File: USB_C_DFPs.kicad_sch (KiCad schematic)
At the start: 34 parts, among them J5 USB_C_Receptacle, J6 USB_C_Receptacle, Q5 IRF7807, U6 LM3478MM_NOPB, U7 SY6280, U8 SY6280

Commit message: Updated schematics
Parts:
- removed C37: 220uF, Capacitor_SMD:CP_Elec_10x10, symbol USB_C_HUB-rescue:CP1-Device
- removed C39: 1nF, Capacitor_SMD:C_0402_1005Metric, symbol Device:C
- removed C40: 22nF, Capacitor_SMD:C_0402_1005Metric, symbol Device:C
- removed C41, C42, C46, C47: 10uF, Capacitor_SMD:C_0603_1608Metric, symbol Device:C_Small
- removed C43: 10pF, Capacitor_SMD:C_0402_1005Metric, symbol Device:C
- removed C44, C45: 100nF, Capacitor_SMD:C_0402_1005Metric, symbol Device:C_Small
- removed C48, C49: 270uF(8mOHM), Capacitor_THT:CP_Radial_D8.0mm_P3.50mm, symbol USB_C_HUB-rescue:CP1-Device
- removed D7: MBRD340, SamacSys_Parts_2:STPS30L30DJFTR, symbol Device:D_Schottky
- removed L2: 1uH_5.6mOHM., Inductor_SMD:L_Sunlord_MWSA1004S, symbol USB_C_HUB-rescue:INDUCTOR_SMALL-OLIMEX_RCL
- removed Q5: IRF7807, symbol Transistor_FET:CSD17579Q5A
- removed R24: 2.55K, Resistor_SMD:R_0603_1608Metric, symbol Device:R_US
- removed R25: 26.7K, Resistor_SMD:R_0603_1608Metric, symbol Device:R_US
- removed R26, R27: 6.8K, Resistor_SMD:R_0603_1608Metric, symbol Device:R_US
- removed R28: 100, Resistor_SMD:R_0603_1608Metric, symbol Device:R_US
- removed R29: 1K, Resistor_SMD:R_0603_1608Metric, symbol Device:R_US
- removed R30: 2.94K, Resistor_SMD:R_0603_1608Metric, symbol Device:R_US
- removed R31: 6m, Resistor_SMD:R_0805_2012Metric, symbol Device:R_US
- removed U6: LM3478MM_NOPB, digikey-footprints:TSSOP-8_W3mm, symbol USB_C_HUB-rescue:LM3478MM_NOPB-dk_PMIC-Voltage-Regulators-DC-DC-Switching-Contr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
- removed U7, U8: SY6280, Package_TO_SOT_SMD:SOT-23-5, symbol USB_C_HUB-rescue:SY6280-usb_hub
- added C37, C41, C42: 0.1μF, Capacitor_SMD:C_0402_1005Metric, symbol Device:C
- added C44, C45: 22μF, Capacitor_SMD:C_0603_1608Metric, symbol Device:C
- added D4: H5VU25U, AZ1045-04F:AZ1045-04F, symbol AZ1045-04F:AZ1045-04F
- added U7: TPS2003CDRCR, DRC10_1P65X2P40_TEX, symbol TPS2003CDRCR:TPS2003CDRCR
- C38: value 100nF -> 0.1μF; LCSC C60474 -> C1525; Part_Number CC0402KRX7R7BB104 -> CL05B104KO5NNNC
- D2, D3: footprint kicad_lceda:DFN2510-10_L2.5-W1.0-P0.50-BL -> AZ1045-04F:AZ1045-04F
- D5: renamed from D4; footprint kicad_lceda:DFN2510-10_L2.5-W1.0-P0.50-BL -> AZ1045-04F:AZ1045-04F
- D6: renamed from D5; footprint kicad_lceda:DFN2510-10_L2.5-W1.0-P0.50-BL -> AZ1045-04F:AZ1045-04F
- D7: renamed from D6; footprint kicad_lceda:DFN2510-10_L2.5-W1.0-P0.50-BL -> AZ1045-04F:AZ1045-04F
- J5, J6: footprint (none) -> USB-C-SMD_TYPE-C-24P-QT:USB-C-SMD_TYPE-C-24P-QT; LCSC (none) -> C2681555; Part_Number (none) -> TYPE-C 24P QT
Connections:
- net +3V3 is gone; now on net USB_DFP1_VBUS: C38.1
- net +5V: now also C42.1, U7.2 (IN)
- net GND: now also C37.2, C41.2, C42.2, C44.2, C45.2, D4.3 (GND), U7.1 (GND), U7.11 (EPAD)
- net USB_DFP0_RX1N: now also D2.5 (I/O_4); no longer D3.4 (I/O_3)
- net USB_DFP0_RX1P: now also D2.4 (I/O_3); no longer D3.5 (I/O_4)
- net USB_DFP0_RX2N: now also D4.1 (I/O_1); no longer D2.4 (I/O_3)
- net USB_DFP0_RX2P: now also D4.2 (I/O_2); no longer D2.5 (I/O_4)
- net USB_DFP0_TX2N: now also D3.4 (I/O_3); no longer D3.2 (I/O_2)
- net USB_DFP0_TX2P: now also D3.5 (I/O_4); no longer D3.1 (I/O_1)
- net USB_DFP0_VBUS: now also C37.1, C45.1, U7.9 (OUT1)
- net USB_DFP1_RX1N: now also D6.2 (I/O_2); no longer D7.4 (I/O_3)
- net USB_DFP1_RX1P: now also D6.1 (I/O_1); no longer D7.5 (I/O_4)
- net USB_DFP1_RX2N: now also D7.1 (I/O_1); no longer D6.4 (I/O_3)
- net USB_DFP1_RX2P: now also D7.2 (I/O_2); no longer D6.5 (I/O_4)
- net USB_DFP1_TX1N: now also D5.5 (I/O_4); no longer D6.2 (I/O_2)
- net USB_DFP1_TX1P: now also D5.4 (I/O_3); no longer D6.1 (I/O_1)
- net USB_DFP1_TX2N: now also D6.4 (I/O_3); no longer D7.2 (I/O_2)
- net USB_DFP1_TX2P: now also D6.5 (I/O_4); no longer D7.1 (I/O_1)
- net USB_DFP1_VBUS: now also C44.1, U7.8 (OUT2)
- removed net USB_DFP0_DM: D5.4 (I/O_3), J5.A7 (D-), J5.B7 (D-)
- removed net USB_DFP0_DP: D5.5 (I/O_4), J5.A6 (D+), J5.B6 (D+)
- removed net USB_DFP1_DM: D5.1 (I/O_1), J6.A7 (D-), J6.B7 (D-)
- removed net USB_DFP1_DP: D5.2 (I/O_2), J6.A6 (D+), J6.B6 (D+)
- new net: C41.1, U7.3 (IN)
- new net USB_DFP0_D1N: D3.2 (I/O_2), J5.A7 (D-)
- new net USB_DFP0_D1P: D3.1 (I/O_1), J5.A6 (D+)
- new net USB_DFP0_D2N: D4.5 (I/O_4), J5.B7 (D-)
- new net USB_DFP0_D2P: D4.4 (I/O_3), J5.B6 (D+)
- new net USB_DFP0_EN: U7.4 (EN1)
- new net USB_DFP0_FLT: U7.10 (*FLT1)
- new net USB_DFP1_D1N: D7.5 (I/O_4), J6.A7 (D-)
- new net USB_DFP1_D1P: D7.4 (I/O_3), J6.A6 (D+)
- new net USB_DFP1_D2N: D5.2 (I/O_2), J6.B7 (D-)
- new net USB_DFP1_D2P: D5.1 (I/O_1), J6.B6 (D+)
- new net USB_DFP1_EN: U7.5 (EN2)
- new net USB_DFP1_FLT: U7.6 (*FLT2)
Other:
- note removed: "Boost Converter 5A 5V"
- note removed: "Iset=6800/rs 1A limit r2=6.8k"
- note removed: "Over-current and short circuit protection"
- note removed: "electrolytic alluminium hv little esr"
- moved on the sheet: J6

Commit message: Continue working on board layout
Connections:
- net GND: now also D2.8 (GND), D3.8 (GND), D4.8 (GND), D5.8 (GND), D6.8 (GND), D7.8 (GND)
- net USB_DFP0_D1N: now also D3.9 (NC)
- net USB_DFP0_D1P: now also D3.10 (NC)
- net USB_DFP0_D2N: now also D4.6 (NC)
- net USB_DFP0_D2P: now also D4.7 (NC)
- net USB_DFP0_RX1N: now also D2.6 (NC)
- net USB_DFP0_RX1P: now also D2.7 (NC)
- net USB_DFP0_RX2N: now also D4.10 (NC)
- net USB_DFP0_RX2P: now also D4.9 (NC)
- net USB_DFP0_TX1N: now also D2.9 (NC)
- net USB_DFP0_TX1P: now also D2.10 (NC)
- net USB_DFP0_TX2N: now also D3.7 (NC)
- net USB_DFP0_TX2P: now also D3.6 (NC)
- net USB_DFP1_D1N: now also D7.6 (NC)
- net USB_DFP1_D1P: now also D7.7 (NC)
- net USB_DFP1_D2N: now also D5.9 (NC)
- net USB_DFP1_D2P: now also D5.10 (NC)
- net USB_DFP1_RX1N: now also D6.9 (NC)
- net USB_DFP1_RX1P: now also D6.10 (NC)
- net USB_DFP1_RX2N: now also D7.10 (NC)
- net USB_DFP1_RX2P: now also D7.9 (NC)
- net USB_DFP1_TX1N: now also D5.6 (NC)
- net USB_DFP1_TX1P: now also D5.7 (NC)
- net USB_DFP1_TX2N: now also D6.7 (NC)
- net USB_DFP1_TX2P: now also D6.6 (NC)

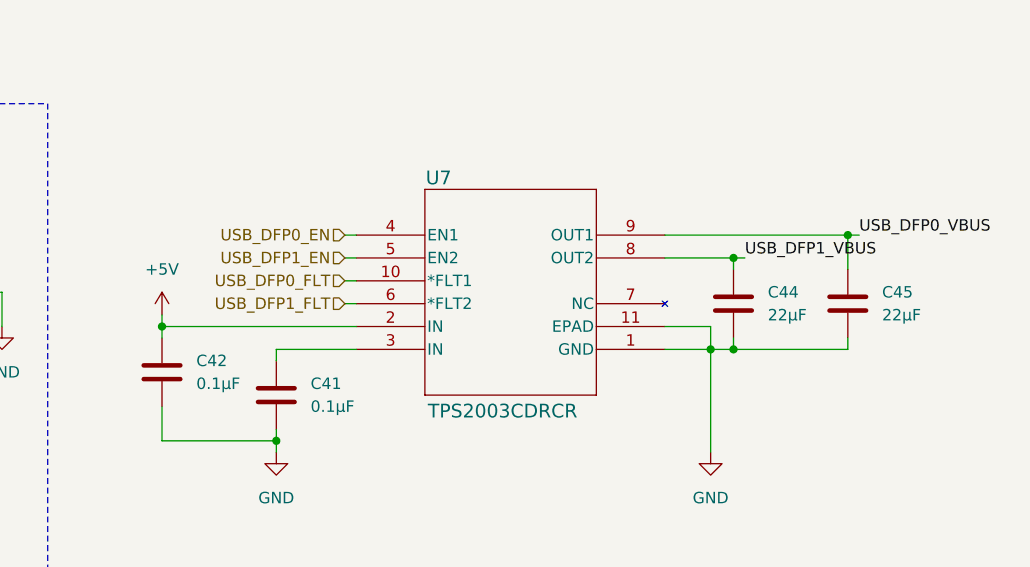
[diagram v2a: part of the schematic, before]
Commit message: Lay out more components
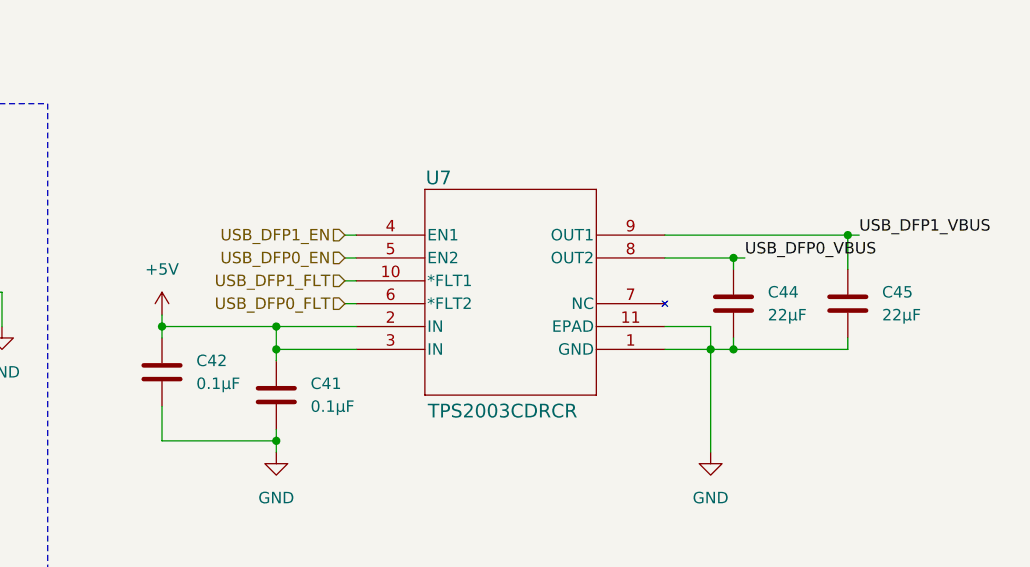
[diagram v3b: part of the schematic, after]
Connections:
- net +5V: now also C41.1, U7.3 (IN)
- net USB_DFP0_EN: now also U7.5 (EN2); no longer U7.4 (EN1)
- net USB_DFP0_FLT: now also U7.6 (*FLT2); no longer U7.10 (*FLT1)
- net USB_DFP0_VBUS: now also C44.1, U7.8 (OUT2); no longer C45.1, U7.9 (OUT1)
- net USB_DFP1_EN: now also U7.4 (EN1); no longer U7.5 (EN2)
- net USB_DFP1_FLT: now also U7.10 (*FLT1); no longer U7.6 (*FLT2)
- net USB_DFP1_VBUS: now also C45.1, U7.9 (OUT1); no longer C44.1, U7.8 (OUT2)
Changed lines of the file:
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@@
+	)
+	(junction
+		(at 200.66 143.51)
+		(diameter 0)
+		(color 0 0 0 0)
 	)
 	(junction
@@
 	)
 	(junction
+		(at 200.66 140.97)
+		(diameter 0)
+		(color 0 0 0 0)
+	)
+	(junction
 		(at 97.79 137.16)
 		(diameter 0)
@@
 	(wire
 		(pts
+			(xy 200.66 140.97) (xy 200.66 143.51)
+		)
+		(stroke
+			(width 0)
+			(type default)
+		)
+	)
+	(wire
+		(pts
 			(xy 86.36 88.9) (xy 90.17 88.9)
 		)
@@
 	(wire
 		(pts
-			(xy 187.96 140.97) (xy 209.55 140.97)
+			(xy 187.96 140.97) (xy 200.66 140.97)
 		)
 		(stroke
@@
 		(pts
 			(xy 45.72 33.02) (xy 49.53 33.02)
+		)
+		(stroke
+			(width 0)
+			(type default)
+		)
+	)
+	(wire
+		(pts
+			(xy 200.66 140.97) (xy 209.55 140.97)
 		)
 		(stroke
@@
 		)
 	)
-	(label "USB_DFP0_VBUS"
+	(label "USB_DFP1_VBUS"
 		(at 265.43 130.81 0)
 		(fields_autoplaced yes)
@@
 		)
 	)
-	(label "USB_DFP1_VBUS"
+	(label "USB_DFP0_VBUS"
 		(at 252.73 133.35 0)
 		(fields_autoplaced yes)
@@
 		)
 	)
-	(hierarchical_label "USB_DFP1_EN"
+	(hierarchical_label "USB_DFP0_EN"
 		(shape input)
 		(at 208.28 133.35 180)
@@
 		)
 	)
-	(hierarchical_label "USB_DFP0_FLT"
+	(hierarchical_label "USB_DFP1_FLT"
 		(shape input)
 		(at 208.28 135.89 180)
@@
 		)
 	)
-	(hierarchical_label "USB_DFP1_FLT"
+	(hierarchical_label "USB_DFP0_FLT"
 		(shape input)
 		(at 208.28 138.43 180)
@@
 		)
 	)
-	(hierarchical_label "USB_DFP0_EN"
+	(hierarchical_label "USB_DFP1_EN"
 		(shape input)
 		(at 208.28 130.81 180)

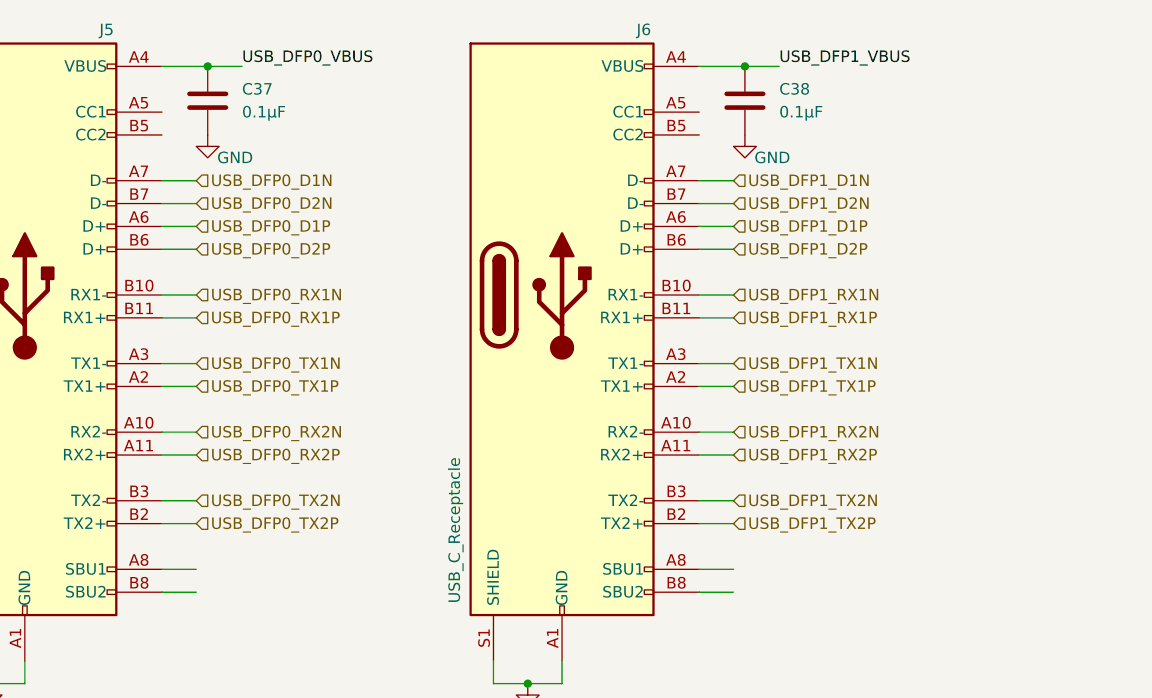
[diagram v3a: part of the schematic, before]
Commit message: Add CC values to DFP ports
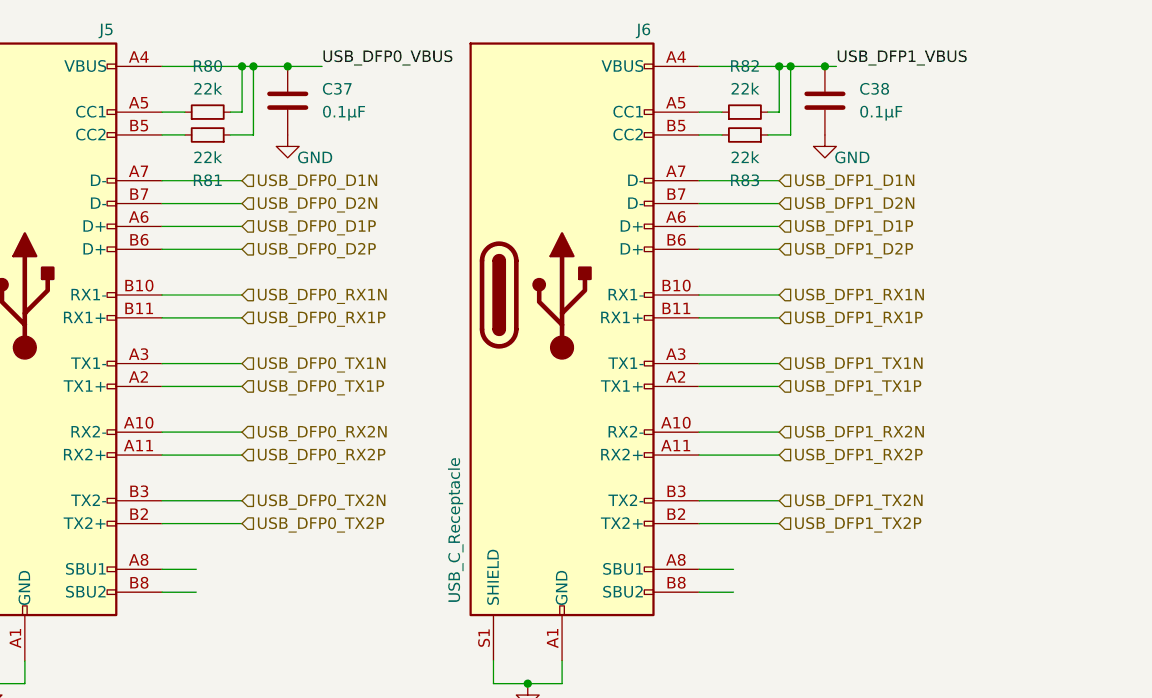
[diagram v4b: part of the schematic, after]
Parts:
- added R80, R81, R82, R83: 22k, Resistor_SMD:R_0402_1005Metric, symbol Device:R_Small
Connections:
- net USB_DFP0_VBUS: now also R80.2, R81.1
- net USB_DFP1_VBUS: now also R82.2, R83.1
- net at J6.A5 (CC1): now also R82.1
- net at J6.B5 (CC2): now also R83.2
- net at J5.A5 (CC1): now also R80.1
- net at J5.B5 (CC2): now also R81.2
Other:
- moved on the sheet: C37, C38

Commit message: Fixed all DRC errors
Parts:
- U7: footprint DRC10_1P65X2P40_TEX -> TPS2003CDRCR:DRC10_1P65X2P40_TEX
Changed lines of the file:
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@@
 			)
 		)
-		(property "Footprint" "DRC10_1P65X2P40_TEX"
+		(property "Footprint" "TPS2003CDRCR:DRC10_1P65X2P40_TEX"
 			(at 209.55 130.81 0)
 			(effects

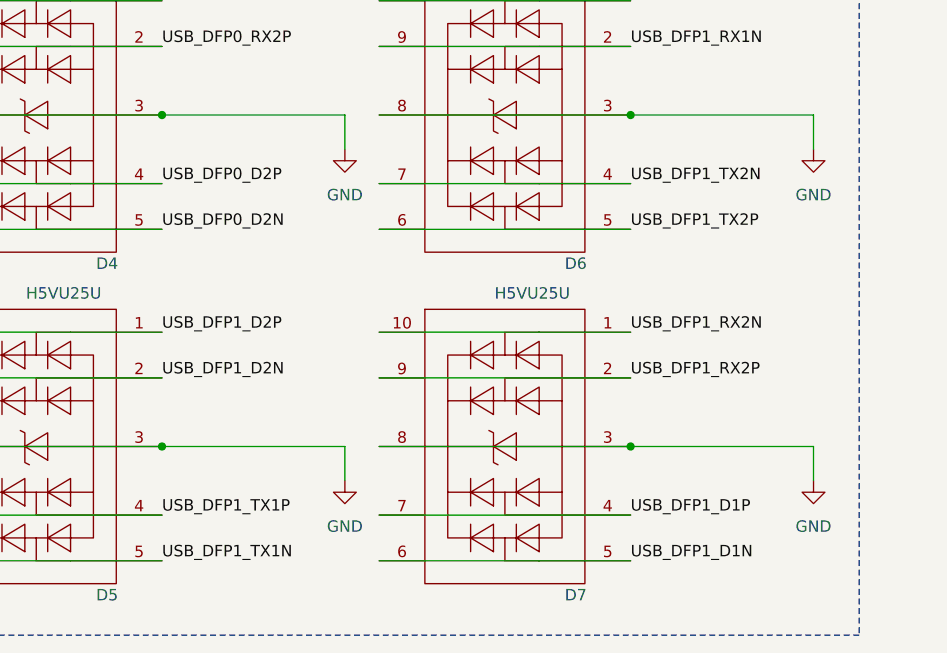
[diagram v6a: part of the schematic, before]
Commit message: pcb: redid layout for USB hub
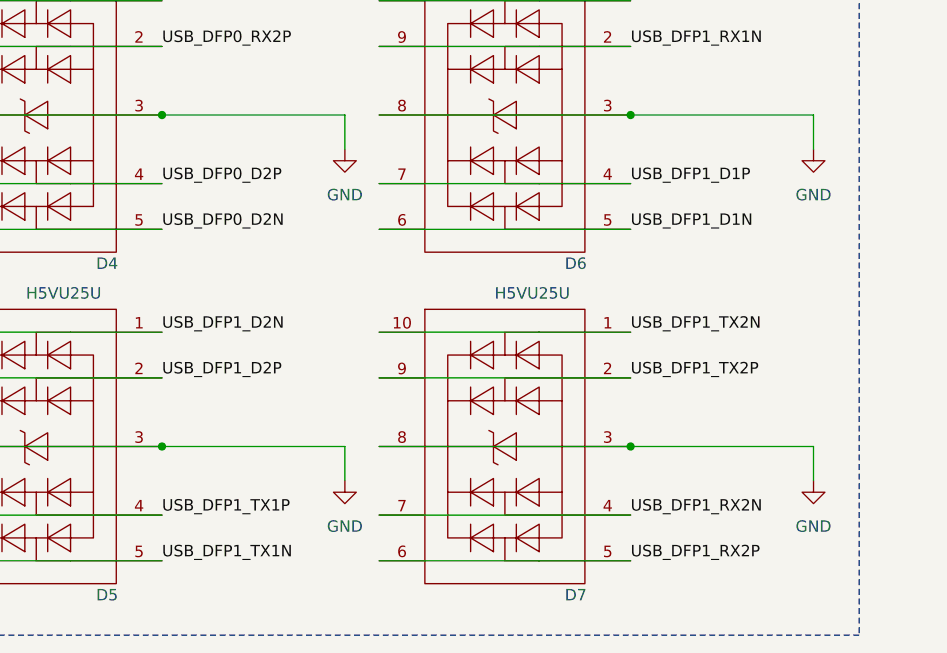
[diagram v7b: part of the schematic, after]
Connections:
- net USB_DFP1_D1N: now also D6.5 (I/O_4), D6.6 (NC); no longer D7.5 (I/O_4), D7.6 (NC)
- net USB_DFP1_D1P: now also D6.4 (I/O_3), D6.7 (NC); no longer D7.4 (I/O_3), D7.7 (NC)
- net USB_DFP1_D2N: now also D5.1 (I/O_1), D5.10 (NC); no longer D5.2 (I/O_2), D5.9 (NC)
- net USB_DFP1_D2P: now also D5.2 (I/O_2), D5.9 (NC); no longer D5.1 (I/O_1), D5.10 (NC)
- net USB_DFP1_RX2N: now also D7.4 (I/O_3), D7.7 (NC); no longer D7.1 (I/O_1), D7.10 (NC)
- net USB_DFP1_RX2P: now also D7.5 (I/O_4), D7.6 (NC); no longer D7.2 (I/O_2), D7.9 (NC)
- net USB_DFP1_TX2N: now also D7.1 (I/O_1), D7.10 (NC); no longer D6.4 (I/O_3), D6.7 (NC)
- net USB_DFP1_TX2P: now also D7.2 (I/O_2), D7.9 (NC); no longer D6.5 (I/O_4), D6.6 (NC)
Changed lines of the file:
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@@
 		)
 	)
-	(label "USB_DFP1_D1N"
+	(label "USB_DFP1_RX2P"
 		(at 149.86 186.69 0)
 		(fields_autoplaced yes)
@@
 		)
 	)
-	(label "USB_DFP1_TX2P"
+	(label "USB_DFP1_D1N"
 		(at 149.86 149.86 0)
 		(fields_autoplaced yes)
@@
 		)
 	)
-	(label "USB_DFP1_D2N"
+	(label "USB_DFP1_D2P"
 		(at 97.79 166.37 0)
 		(fields_autoplaced yes)
@@
 		)
 	)
-	(label "USB_DFP1_D1P"
+	(label "USB_DFP1_RX2N"
 		(at 149.86 181.61 0)
 		(fields_autoplaced yes)
@@
 		)
 	)
-	(label "USB_DFP1_RX2N"
+	(label "USB_DFP1_TX2N"
 		(at 149.86 161.29 0)
 		(fields_autoplaced yes)
@@
 		)
 	)
-	(label "USB_DFP1_D2P"
+	(label "USB_DFP1_D2N"
 		(at 97.79 161.29 0)
 		(fields_autoplaced yes)
@@
 		)
 	)
-	(label "USB_DFP1_TX2N"
+	(label "USB_DFP1_D1P"
 		(at 149.86 144.78 0)
 		(fields_autoplaced yes)
@@
 		)
 	)
-	(label "USB_DFP1_RX2P"
+	(label "USB_DFP1_TX2P"
 		(at 149.86 166.37 0)
 		(fields_autoplaced yes)
